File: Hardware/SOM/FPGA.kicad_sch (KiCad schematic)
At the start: 83 parts, among them U1 LFE5UM5G-85F

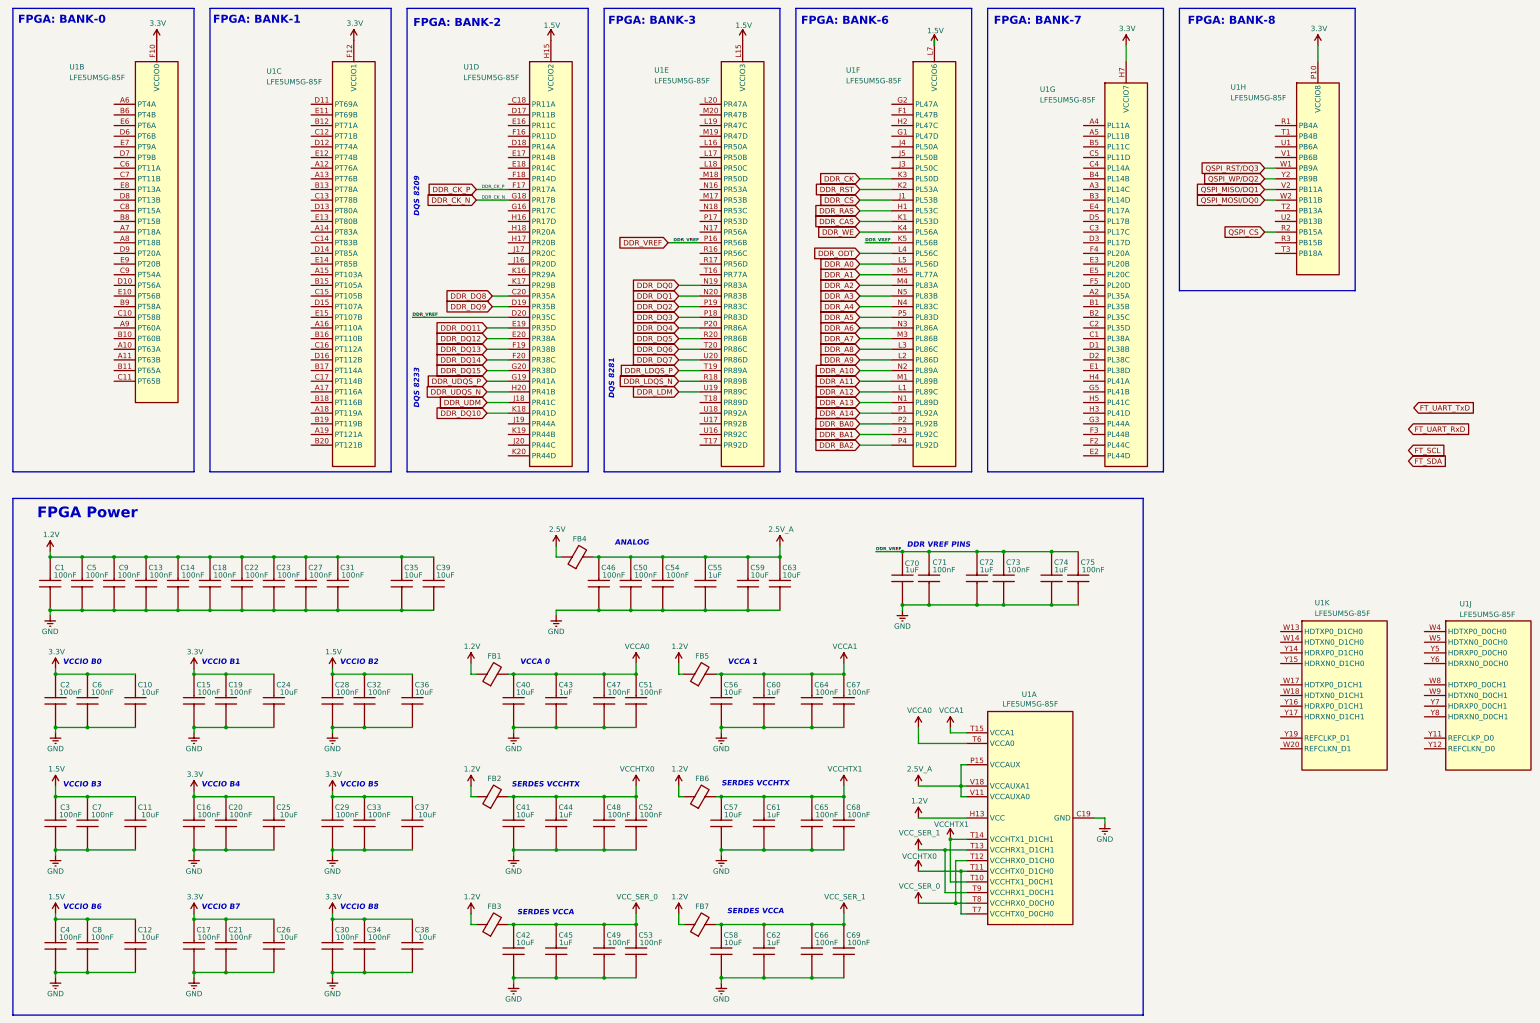
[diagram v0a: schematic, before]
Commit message: SOM stack-up JLC06161H-3313
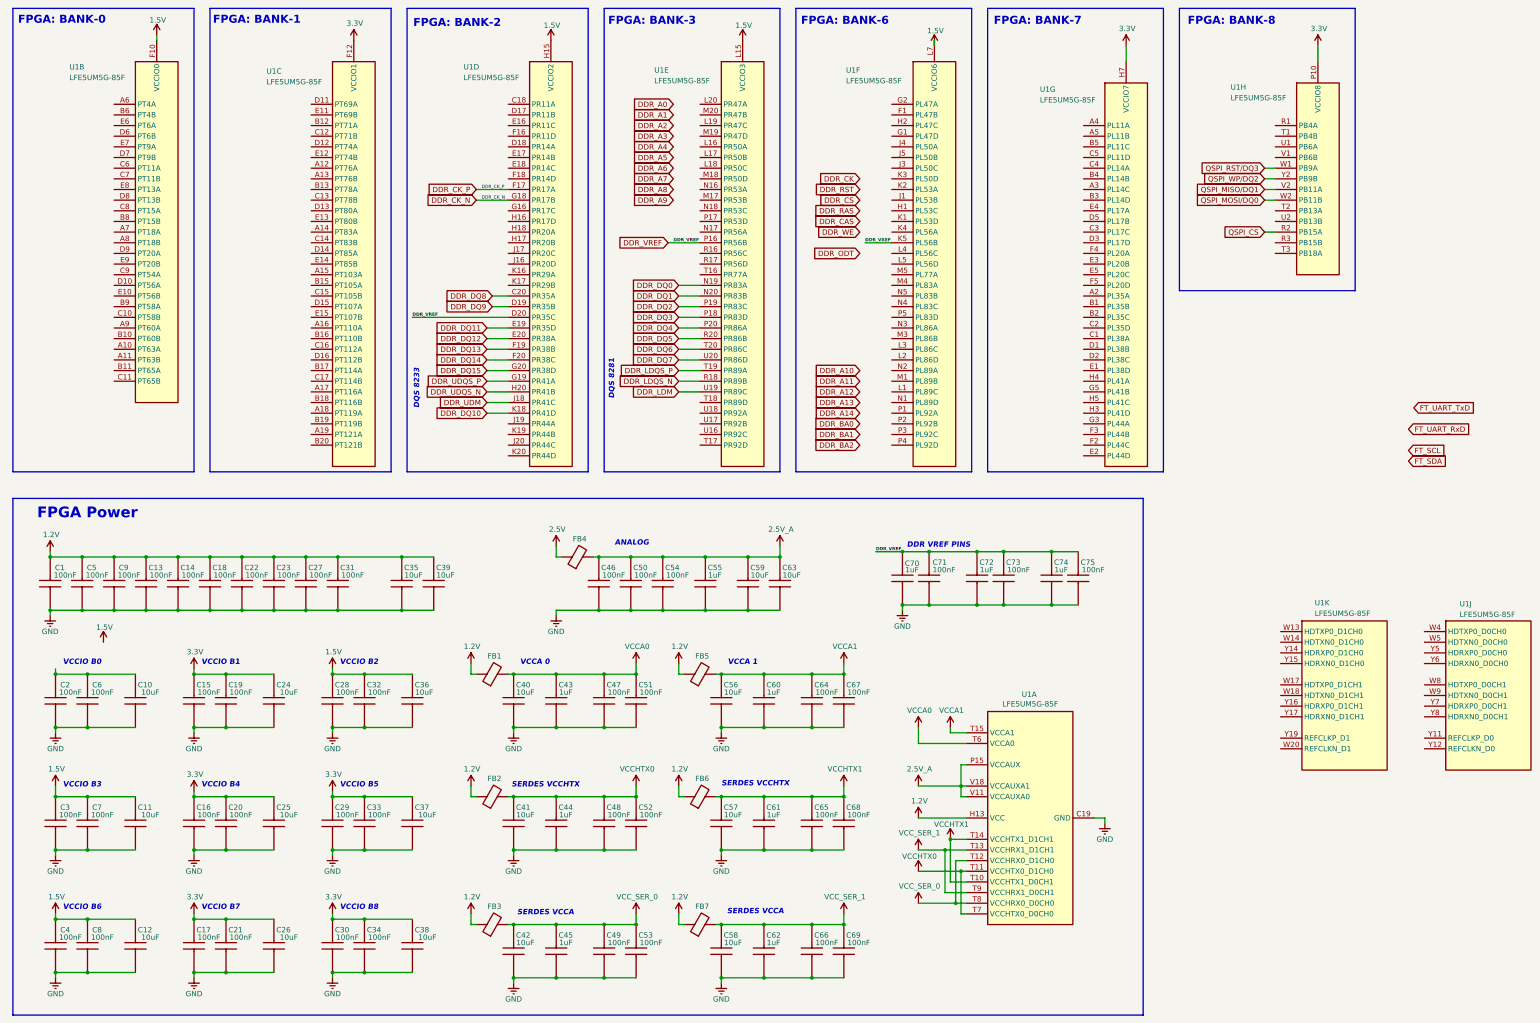
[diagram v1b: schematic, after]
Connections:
- net 1.5V: now also U1.F10 (VCCIO0), U1.F9 (VCCIO0)
- net 3.3V: no longer C10.2, C2.2, C6.2, U1.F10 (VCCIO0), U1.F9 (VCCIO0)
- net DDR_A0: no longer U1.L5 (PL56D)
- net DDR_A1: no longer U1.M5 (PL77A)
- net DDR_A10: no longer U1.N2 (PL89A)
- net DDR_A11: no longer U1.M1 (PL89B)
- net DDR_A12: no longer U1.L1 (PL89C)
- net DDR_A13: no longer U1.N1 (PL89D)
- net DDR_A14: no longer U1.P1 (PL92A)
- net DDR_A2: no longer U1.M4 (PL83A)
- net DDR_A3: no longer U1.N5 (PL83B)
- net DDR_A4: no longer U1.N4 (PL83C)
- net DDR_A5: no longer U1.P5 (PL83D)
- net DDR_A6: no longer U1.N3 (PL86A)
- net DDR_A7: no longer U1.M3 (PL86B)
- net DDR_A8: no longer U1.L3 (PL86C)
- net DDR_A9: no longer U1.L2 (PL86D)
- net DDR_BA0: no longer U1.P2 (PL92B)
- net DDR_BA1: no longer U1.P3 (PL92C)
- net DDR_BA2: no longer U1.P4 (PL92D)
- net DDR_CAS: no longer U1.K1 (PL53D)
- net DDR_CK: no longer U1.K3 (PL50D)
- net DDR_CS: no longer U1.J1 (PL53B)
- net DDR_ODT: no longer U1.L4 (PL56C)
- net DDR_RAS: no longer U1.H1 (PL53C)
- net DDR_RST: no longer U1.K2 (PL53A)
- net DDR_WE: no longer U1.K4 (PL56A)
- new net: C10.2, C2.2, C6.2
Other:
- note removed: "DQS 8209"

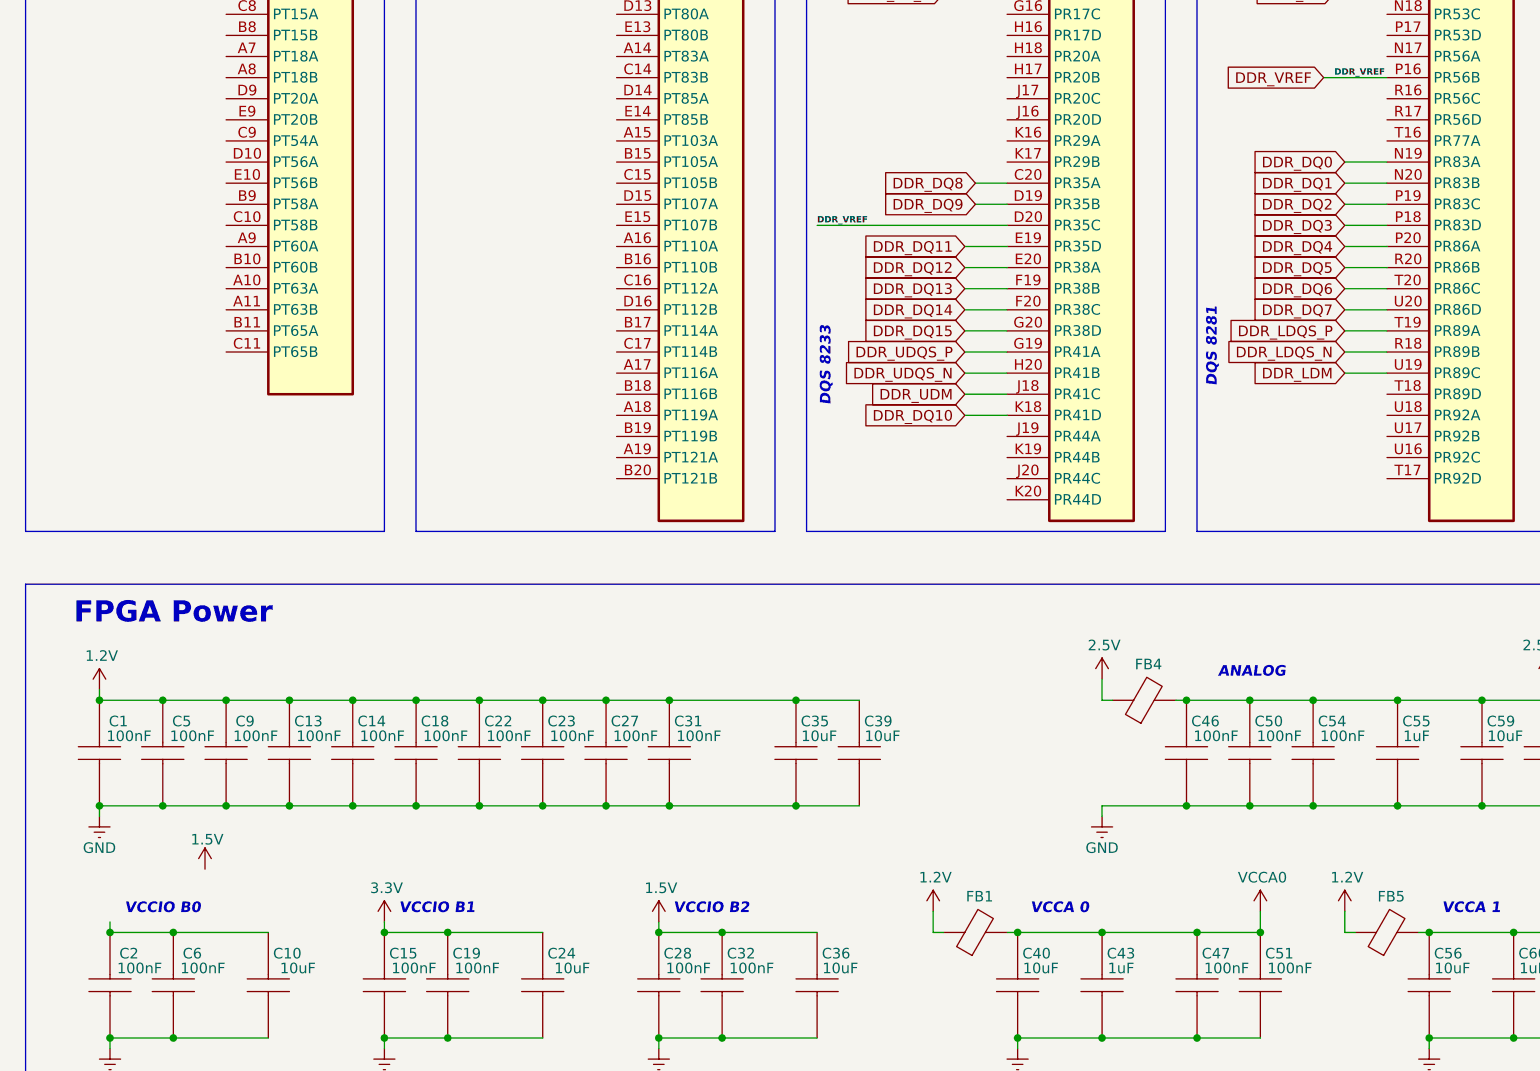
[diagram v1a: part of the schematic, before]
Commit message: some net names added
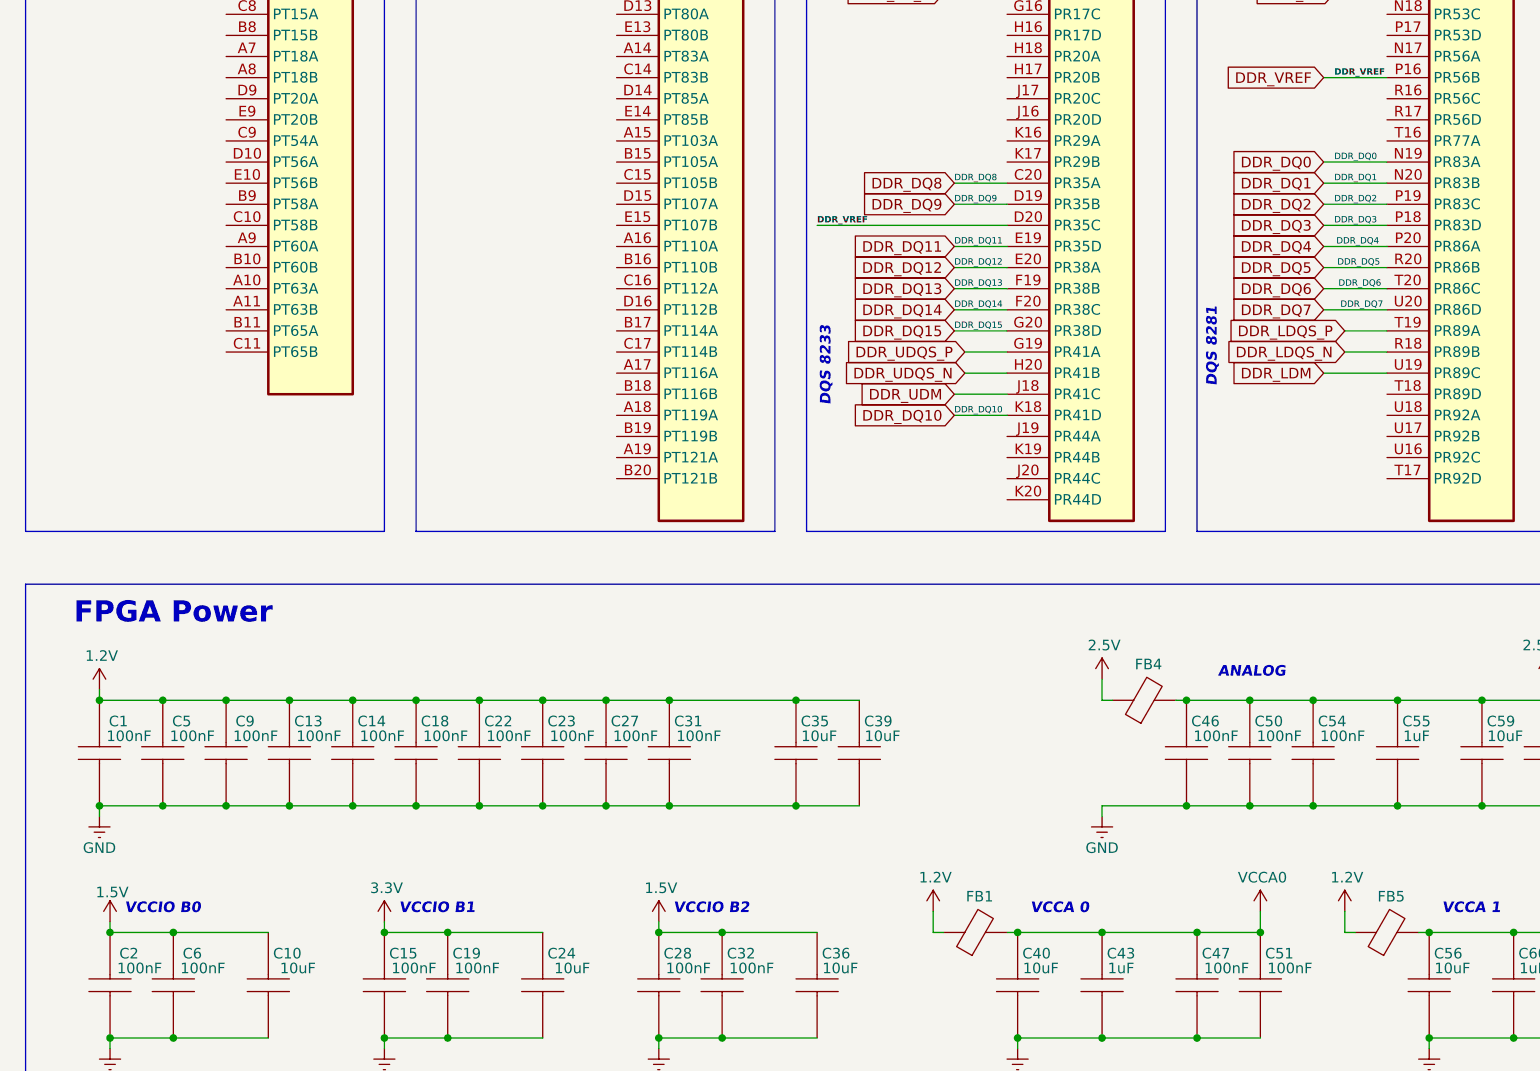
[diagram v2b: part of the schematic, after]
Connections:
- net 1.5V: now also C10.2, C2.2, C6.2
